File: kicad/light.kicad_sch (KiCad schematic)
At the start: 139 parts, among them J2 USB_C_Receptacle_USB2.0_16P, J3 Barrell Jack, J4 01x04, J5 SM03B-SRSS-TB, J6 SM03B-SRSS-TB, J9 Conn_01x09_MountingPin, Q1 NMOS, Q2 NMOS, Q3 NMOS, SW1 Boot, SW3 On/Off, SW4 Mode, U1 RP2350A-QFN60, U10 MAX6816, U2 TPS5405DR, U3 W25Q128JVS, U4 LBEE5KL1YN-814, U5 TPS2115ADRBR, U6 TPS2115ADRBR, U7 HDC1080, U8 MAX6816, U9 MAX6816, Y1 ABM8-272-T3

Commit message: finish routing
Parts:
- removed JP1: VBUS, Jumper:SolderJumper-2_P1.3mm_Open_RoundedPad1.0x1.5mm, symbol Jumper:SolderJumper_2_Open
- removed JP2: PWR_STAT, Jumper:SolderJumper-2_P1.3mm_Bridged_RoundedPad1.0x1.5mm, symbol Jumper:SolderJumper_2_Bridged
- removed R20: 10K, Resistor_SMD:R_0402_1005Metric, symbol Device:R
- removed R21: 5.6K, Resistor_SMD:R_0402_1005Metric, symbol Device:R
- removed R23: 100K, Resistor_SMD:R_0402_1005Metric, symbol Device:R
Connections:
- net GPIO0: now also J9.3 (Pin_3); no longer J9.1 (Pin_1)
- net GPIO2: now also J9.1 (Pin_1); no longer J9.3 (Pin_3)
- net WE_SCL: now also U1.10 (GPIO7); no longer U1.33 (GPIO21)
- net WE_SDA: now also U1.9 (GPIO6); no longer U1.32 (GPIO20)
- net at U1.12 (GPIO8): no longer R4.1
- net PWR_STAT: no longer names the net of U1.15 (GPIO11)
- net WL_GPIO2: no longer names the net of U4.17 (WL_GPIO_2)
- new net: R4.1, U1.32 (GPIO20)
- no-connect marks 24 -> 27
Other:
- note removed: "PWR_STAT is HIGH when VREG5 is in use LOW, when VBUS is in use; this serves as an indicator of when USB is connected"
- moved on the sheet: R4

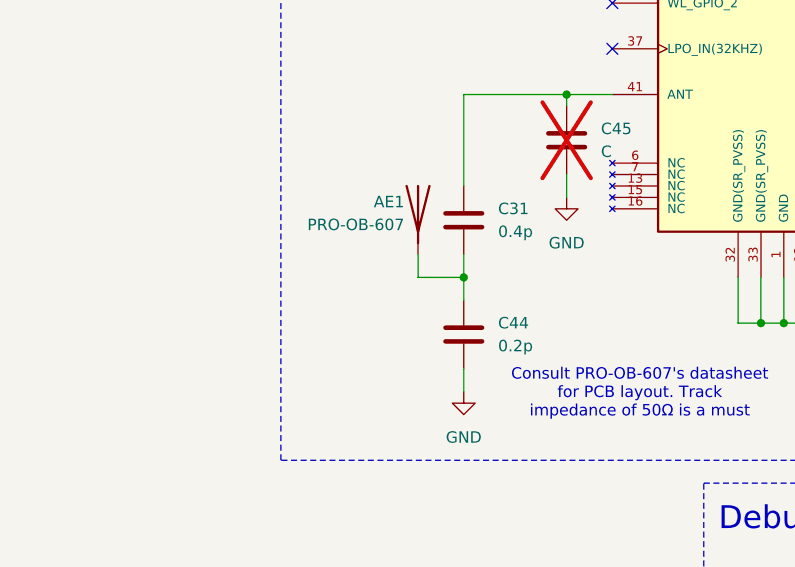
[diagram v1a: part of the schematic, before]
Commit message: route antenna!!! oficially routed the hole board; also solved remaining DRC errors
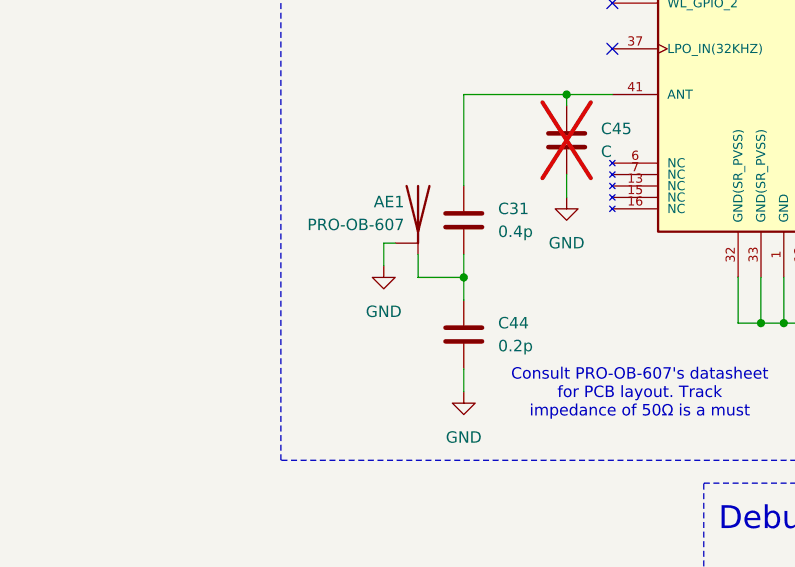
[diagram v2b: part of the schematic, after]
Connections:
- net GND: now also AE1.1 (GND)
- net at C31.2, C44.1: now also AE1.2 (RF_Feed); no longer AE1.1 (A)
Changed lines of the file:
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@@
 	(wire
 		(pts
+			(xy 251.46 397.51) (xy 250.19 397.51)
+		)
+		(stroke
+			(width 0)
+			(type default)
+		)
+	)
+	(wire
+		(pts
 			(xy 488.95 278.13) (xy 500.38 278.13)
 		)
@@
 	(wire
 		(pts
+			(xy 250.19 397.51) (xy 250.19 400.05)
+		)
+		(stroke
+			(width 0)
+			(type default)
+		)
+	)
+	(wire
+		(pts
 			(xy 342.9 335.28) (xy 356.87 335.28)
 		)
@@
 	)
 	(symbol
+		(lib_id "power:GND")
+		(at 250.19 400.05 0)
+		(unit 1)
+		(exclude_from_sim no)
+		(in_bom yes)
+		(on_board yes)
+		(dnp no)
+		(fields_autoplaced yes)
+		(property "Reference" "#PWR051"
+			(at 250.19 406.4 0)
+			(effects
+				(font
+					(size 1.27 1.27)
+				)
+				(hide yes)
+			)
+		)
+		(property "Value" "GND"
+			(at 250.19 405.13 0)
+			(effects
+				(font
+					(size 1.27 1.27)
+				)
+			)
+		)
+		(property "Footprint" ""
+			(at 250.19 400.05 0)
+			(effects
+				(font
+					(size 1.27 1.27)
+				)
+				(hide yes)
+			)
+		)
+		(property "Datasheet" ""
+			(at 250.19 400.05 0)
+			(effects
+				(font
+					(size 1.27 1.27)
+				)
+				(hide yes)
+			)
+		)
+		(property "Description" "Power symbol creates a global label with name \"GND\" , ground"
+			(at 250.19 400.05 0)
+			(effects
+				(font
+					(size 1.27 1.27)
+				)
+				(hide yes)
+			)
+		)
+		(pin "1"
+		)
+		(instances
+			(project "light"
+				(path "/fbb17af3-099c-429d-b186-ab4e8e0fdddf"
+					(reference "#PWR051")
+					(unit 1)
+				)
+			)
+		)
+	)
+	(symbol
 		(lib_id "Interface:MAX6816")
 		(at 500.38 213.36 0)
@@
 		(pin "1"
 		)
+		(pin "2"
+		)
 		(instances

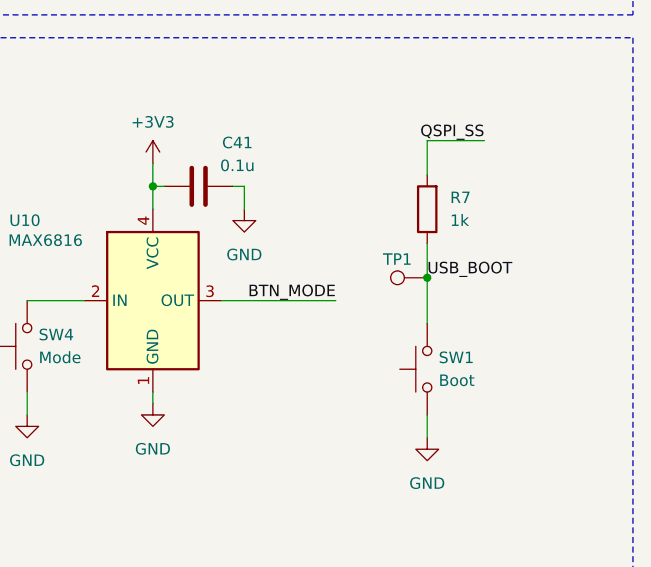
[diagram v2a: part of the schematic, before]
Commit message: add  silkscreen labels and graphics
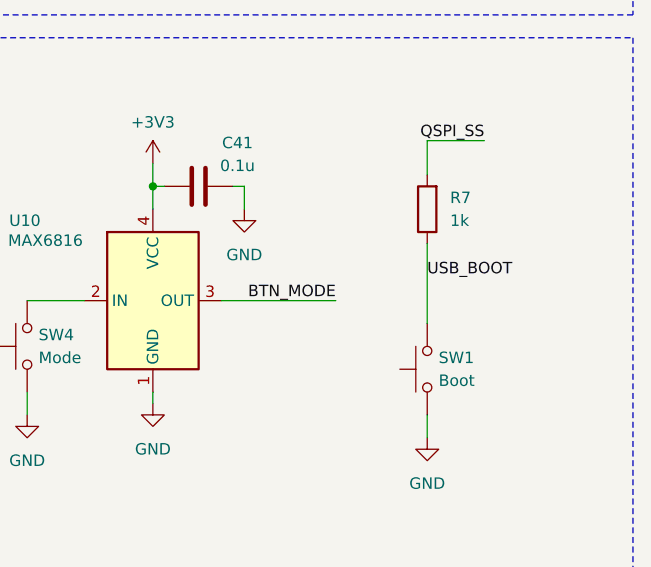
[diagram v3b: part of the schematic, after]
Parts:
- removed TP1: TestPoint, TestPoint:TestPoint_Pad_D1.0mm, symbol Connector:TestPoint
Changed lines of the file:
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@@
 	)
 	(junction
-		(at 613.41 212.09)
-		(diameter 0)
-		(color 0 0 0 0)
-	)
-	(junction
 		(at 476.25 293.37)
 		(diameter 0)
@@
 	(wire
 		(pts
-			(xy 613.41 208.28) (xy 613.41 212.09)
-		)
-		(stroke
-			(width 0)
-			(type default)
-		)
-	)
-	(wire
-		(pts
 			(xy 364.49 349.25) (xy 351.79 349.25)
 		)
@@
 	(wire
 		(pts
-			(xy 613.41 212.09) (xy 613.41 217.17)
+			(xy 613.41 208.28) (xy 613.41 217.17)
 		)
 		(stroke
@@
 					(unit 1)
 				)
-			)
-		)
-	)
-	(symbol
-		(lib_id "Connector:TestPoint")
-		(at 613.41 212.09 90)
-		(unit 1)
-		(exclude_from_sim no)
-		(in_bom yes)
-		(on_board yes)
-		(dnp no)
-		(property "Reference" "TP1"
-			(at 610.108 210.058 90)
-			(effects
-				(font
-					(size 1.27 1.27)
-				)
-			)
-		)
-		(property "Value" "TestPoint"
-			(at 602.488 212.852 90)
-			(effects
-				(font
-					(size 1.27 1.27)
-				)
-				(hide yes)
-			)
-		)
-		(property "Footprint" "TestPoint:TestPoint_Pad_D1.0mm"
-			(at 613.41 207.01 0)
-			(effects
-				(font
-					(size 1.27 1.27)
-				)
-				(hide yes)
-			)
-		)
-		(property "Datasheet" "~"
-			(at 613.41 207.01 0)
-			(effects
-				(font
-					(size 1.27 1.27)
-				)
-				(hide yes)
-			)
-		)
-		(property "Description" "test point"
-			(at 613.41 212.09 0)
-			(effects
-				(font
-					(size 1.27 1.27)
-				)
-				(hide yes)
-			)
-		)
-		(pin "1"
-		)
-		(instances
-			(project "light"
-				(path "/fbb17af3-099c-429d-b186-ab4e8e0fdddf"
-					(reference "TP1")
-					(unit 1)
-				)

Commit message: create new footprint for mounting hole link it to a schematic symbol; solve DRC errors
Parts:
- added H1, H2, H3, H4: MountingHole, MountingHole:MountingHole_1.6mm, symbol Mechanical:MountingHole
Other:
- note added: "JST-SH"
- note added: "UART JST-SH"
- note removed: "JST SH"
- note removed: "UART JST"
- moved on the sheet: AE1, C1, C10, C11, C12, C13, C14, C15, C16, C17, C18, C19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

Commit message: general stuff
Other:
- note added: "2.4mm holes"
- note added: "Mounting Holes"
- note added: "UART"
- note removed: "Hole pins"
- note removed: "UART JST-SH"
- moved on the sheet: C1, C24, C35, C36, C37, C38, D68, D69, D73, H1, H2, H3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

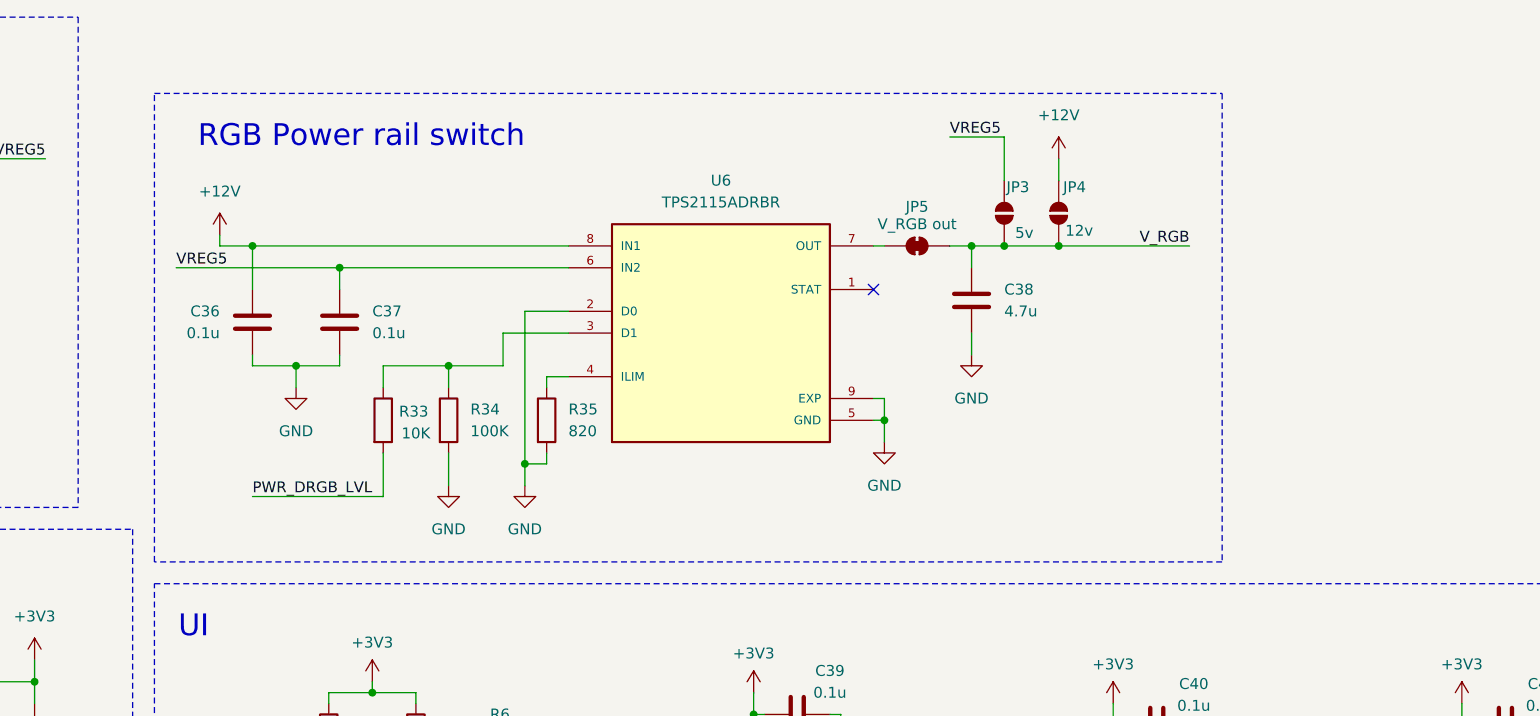
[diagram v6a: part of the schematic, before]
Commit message: replace the power switch with the TPS2120
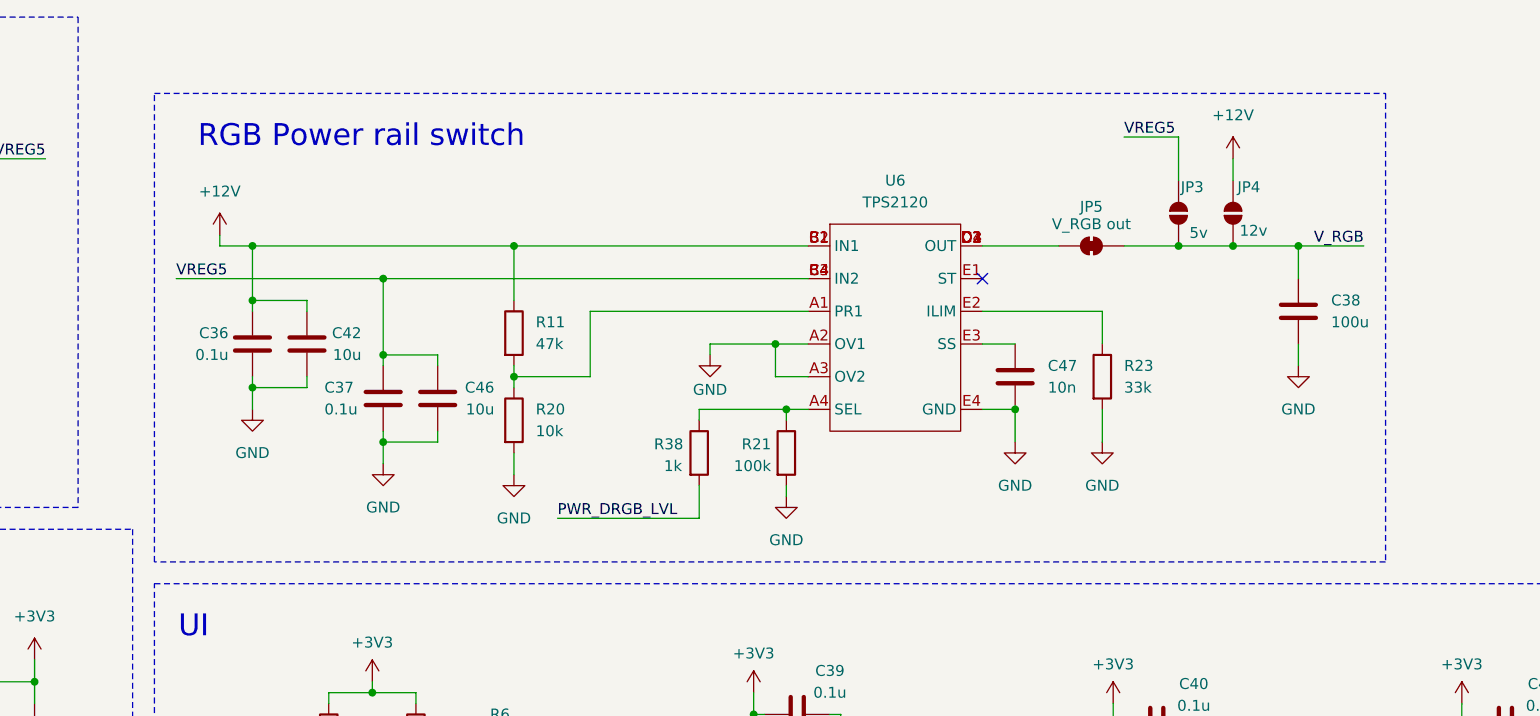
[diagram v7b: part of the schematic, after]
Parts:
- removed R33: 10K, Capacitor_SMD:C_0402_1005Metric, symbol Device:R
- removed R34: 100K, Capacitor_SMD:C_0402_1005Metric, symbol Device:R
- removed R35: 820, Capacitor_SMD:C_0402_1005Metric, symbol Device:R
- removed U6: TPS2115ADRBR, TPS2115ADRBR:SON65P300X300X100-9N, symbol TPS2115ADRBR:TPS2115ADRBR
- added C42, C46: 10u, Capacitor_SMD:C_0201_0603Metric, symbol Device:C
- added C47: 10n, symbol Device:C
- added R11: 47k, symbol Device:R
- added R20: 10k, symbol Device:R
- added R21: 100k, symbol Device:R
- added R23: 33k, symbol Device:R
- added R38: 1k, Capacitor_SMD:C_0402_1005Metric, symbol Device:R
- added U6: TPS2120, TPS2120:TPS2120YFP, symbol TPS2120:TPS2120
- C38: value 4.7u -> 100u
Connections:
- net +12V: now also C42.1, R11.1, U6.B1 (IN1), U6.B2 (IN1), U6.C1 (IN1)
- net GND: now also C42.2, C46.2, C47.2, R20.2, R21.2, R23.2, U6.A2 (OV1), U6.A3 (OV2), U6.E4 (GND)
- net PWR_DRGB_LVL: now also R38.2
- net VREG5: now also C46.1, U6.B3 (IN2), U6.B4 (IN2), U6.C4 (IN2)
- net at JP5.1 (A): now also U6.C2 (OUT), U6.C3 (OUT), U6.D1 (OUT), U6.D2 (OUT), U6.D3 (OUT), U6.D4 (OUT)
- new net: R11.2, R20.1, U6.A1 (PR1)
- new net: R21.1, R38.1, U6.A4 (SEL)
- new net: R23.1, U6.E2 (ILIM)
- new net: C47.1, U6.E3 (SS)
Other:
- moved on the sheet: C36, C37, C38, JP3, JP4, JP5

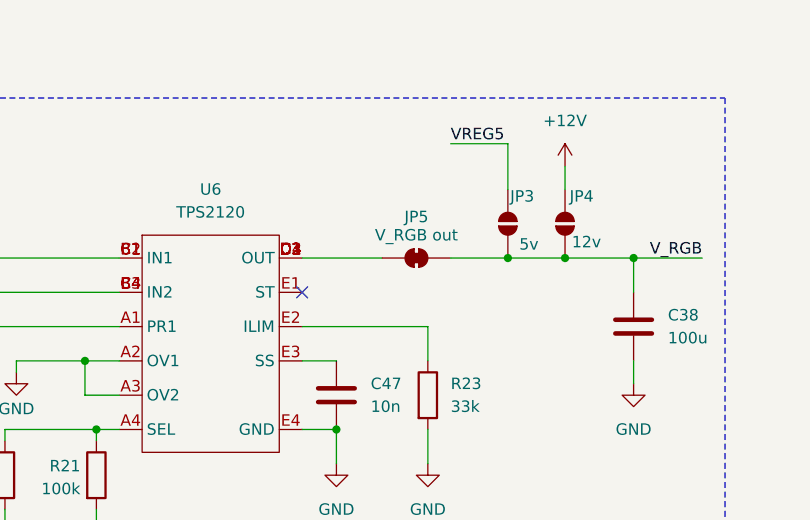
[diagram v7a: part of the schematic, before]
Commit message: layout pwr switch on PCB
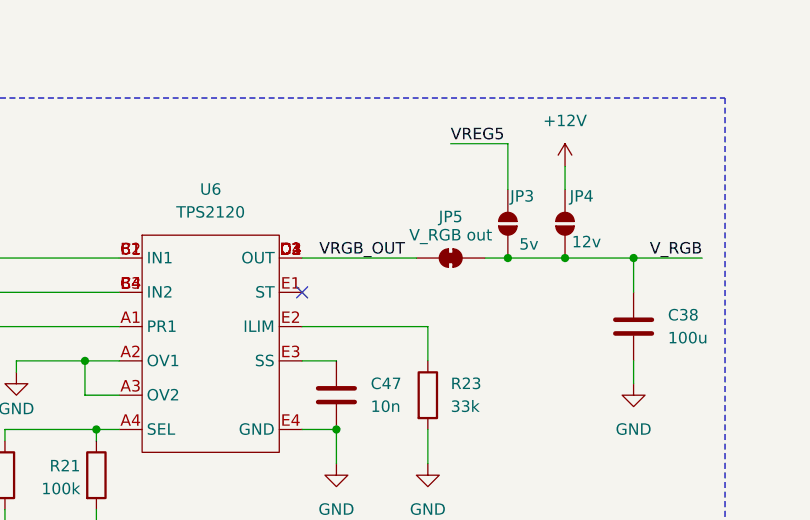
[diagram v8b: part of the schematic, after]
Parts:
- C47: footprint (none) -> Capacitor_SMD:C_0201_0603Metric
- R11, R20, R21, R23: footprint (none) -> Resistor_SMD:R_0201_0603Metric
- R27, R28, R29, R30, R31, R32: footprint Capacitor_SMD:C_0402_1005Metric -> Resistor_SMD:R_0402_1005Metric
- R38: footprint Capacitor_SMD:C_0402_1005Metric -> Resistor_SMD:R_0201_0603Metric
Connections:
- net VRGB_OUT: now reaches JP5.1 (A), U6.C2 (OUT), U6.C3 (OUT), U6.D1 (OUT), U6.D2 (OUT), U6.D3 (OUT), U6.D4 (OUT)
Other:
- moved on the sheet: JP5
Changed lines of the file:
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@@
 	(wire
 		(pts
-			(xy 403.86 55.88) (xy 412.75 55.88)
+			(xy 403.86 55.88) (xy 416.56 55.88)
 		)
 		(stroke
@@
 	(wire
 		(pts
-			(xy 420.37 55.88) (xy 426.72 55.88)
+			(xy 424.18 55.88) (xy 426.72 55.88)
 		)
 		(stroke
@@
 		)
 	)
+	(label "VRGB_OUT"
+		(at 415.29 55.88 180)
+		(effects
+			(font
+				(size 1.27 1.27)
+			)
+			(justify right bottom)
+		)
+	)
 	(label "WL_CLK"
 		(at 261.62 283.21 180)
@@
 			)
 		)
-		(property "Footprint" "Capacitor_SMD:C_0402_1005Metric"
+		(property "Footprint" "Resistor_SMD:R_0402_1005Metric"
 			(at 502.412 245.11 90)
 			(effects
@@
 			)
 		)
-		(property "Footprint" "Capacitor_SMD:C_0402_1005Metric"
+		(property "Footprint" "Resistor_SMD:R_0402_1005Metric"
 			(at 490.982 245.11 90)
 			(effects
@@
 			)
 		)
-		(property "Footprint" ""
+		(property "Footprint" "Resistor_SMD:R_0201_0603Metric"
 			(at 347.472 76.2 90)
 			(effects
@@
 			)
 		)
-		(property "Footprint" "Capacitor_SMD:C_0402_1005Metric"
+		(property "Footprint" "Resistor_SMD:R_0402_1005Metric"
 			(at 480.06 218.948 90)
 			(effects
@@
 			)
 		)
-		(property "Footprint" "Capacitor_SMD:C_0402_1005Metric"
+		(property "Footprint" "Resistor_SMD:R_0402_1005Metric"
 			(at 513.842 245.11 90)
 			(effects
@@
 	(symbol
 		(lib_id "Jumper:SolderJumper_2_Bridged")
-		(at 416.56 55.88 0)
+		(at 420.37 55.88 0)
 		(unit 1)
 		(exclude_from_sim no)
@@
 		(dnp no)
 		(property "Reference" "JP5"
-			(at 416.56 51.308 0)
+			(at 420.37 51.308 0)
 			(effects
 				(font
@@
 		)
 		(property "Value" "V_RGB out"
-			(at 416.56 53.34 0)
+			(at 420.37 53.34 0)
 			(effects
 				(font
@@
 		)
 		(property "Footprint" "Jumper:SolderJumper-2_P1.3mm_Bridged_RoundedPad1.0x1.5mm"
-			(at 416.56 55.88 0)
+			(at 420.37 55.88 0)
 			(effects
 				(font
@@
 		)
 		(property "Datasheet" "~"
-			(at 416.56 55.88 0)
+			(at 420.37 55.88 0)
 			(effects
 				(font
@@
 		)
 		(property "Description" "Solder Jumper, 2-pole, closed/bridged"
-			(at 416.56 55.88 0)
+			(at 420.37 55.88 0)
 			(effects
 				(font
@@
 			)
 		)
-		(property "Footprint" ""
+		(property "Footprint" "Resistor_SMD:R_0201_0603Metric"
 			(at 416.052 71.12 90)
 			(effects
@@
 			)
 		)
-		(property "Footprint" ""
+		(property "Footprint" "Capacitor_SMD:C_0201_0603Metric"
 			(at 408.6352 74.93 0)
 			(effects
@@
 			)
 		)
-		(property "Footprint" "Capacitor_SMD:C_0402_1005Metric"
+		(property "Footprint" "Resistor_SMD:R_0402_1005Metric"
 			(at 480.06 229.108 90)
 			(effects
@@
 			)
 		)
-		(property "Footprint" "Capacitor_SMD:C_0402_1005Metric"
+		(property "Footprint" "Resistor_SMD:R_0402_1005Metric"
 			(at 480.06 239.268 90)
 			(effects
@@
 			)
 		)
-		(property "Footprint" "Capacitor_SMD:C_0402_1005Metric"
+		(property "Footprint" "Resistor_SMD:R_0201_0603Metric"
 			(at 369.062 80.01 90)
 			(effects
@@
 			)
 		)
-		(property "Footprint" ""
+		(property "Footprint" "Resistor_SMD:R_0201_0603Metric"
 			(at 379.222 80.01 90)
 			(effects
@@
 			)
 		)
-		(property "Footprint" ""
+		(property "Footprint" "Resistor_SMD:R_0201_0603Metric"
 			(at 347.472 66.04 90)
 			(effects
